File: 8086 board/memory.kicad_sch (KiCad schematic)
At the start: 49 parts, among them U10 74AC573, U11 74HC138, U12 74HC138, U13 CXK58257AM, U14 IS61C256AH, U15 IS61C256AH, U16 IS61C256AH, U17 IS61C256AH, U18 IS61C3216, U19 AM29F002, U2 74AC00, U20 AM29F002, U21 28F400B5, U3 74HC14, U8 74AC573, U9 74AC573

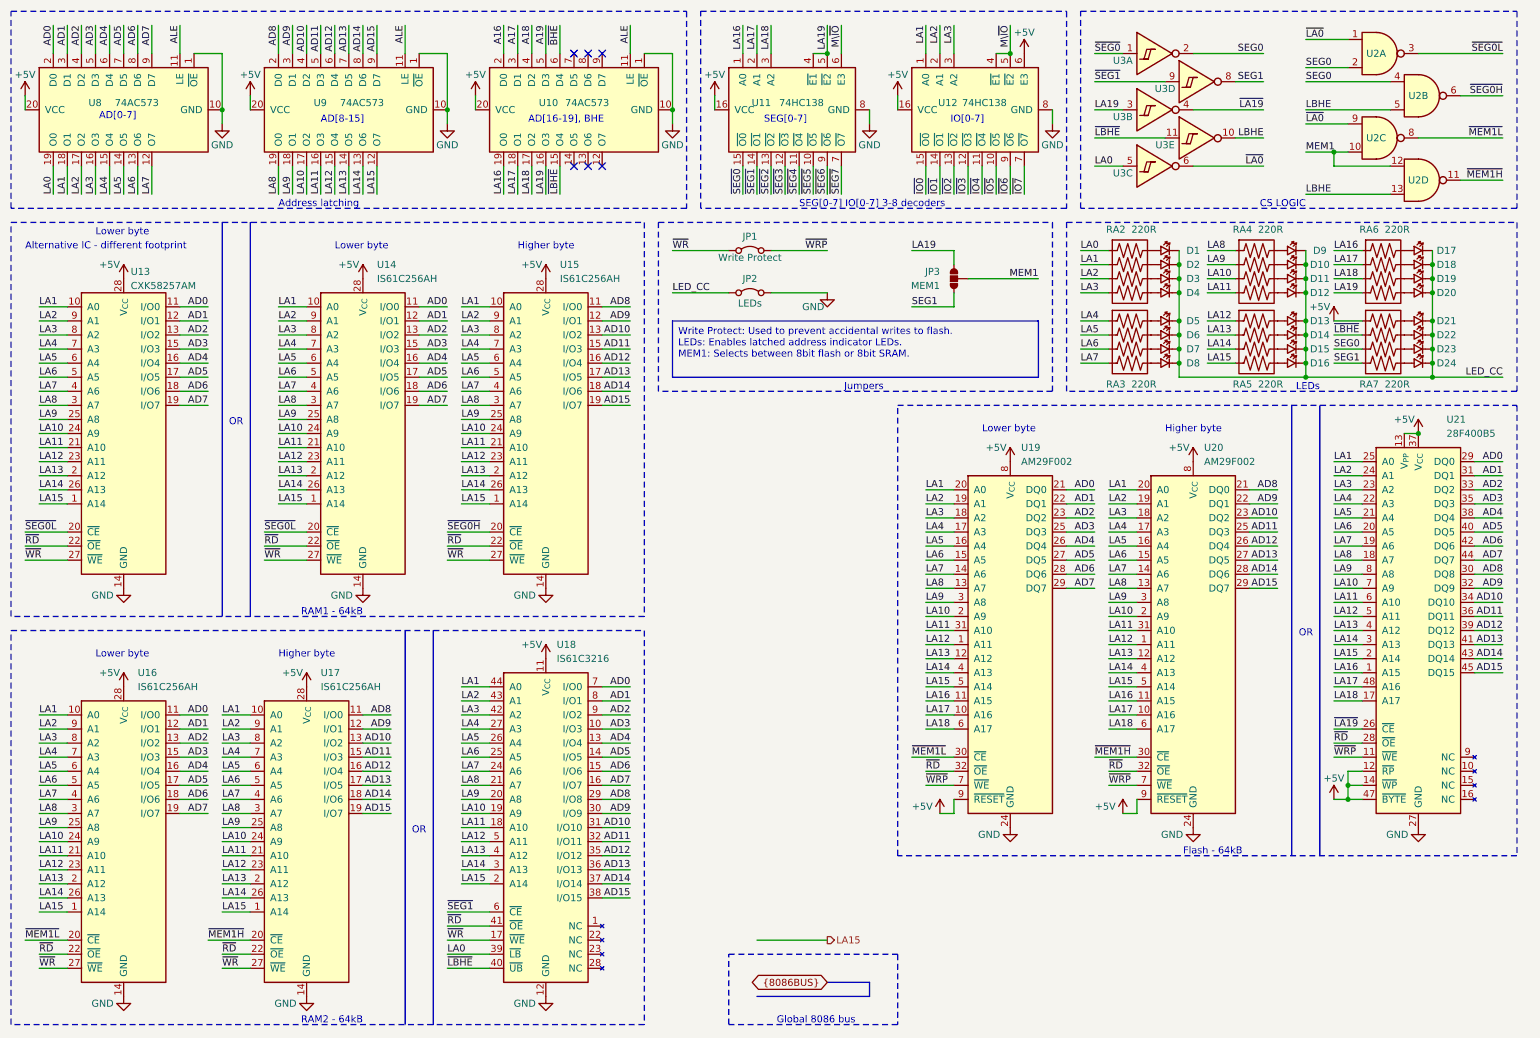
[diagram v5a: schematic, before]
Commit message: change schematic to use new components
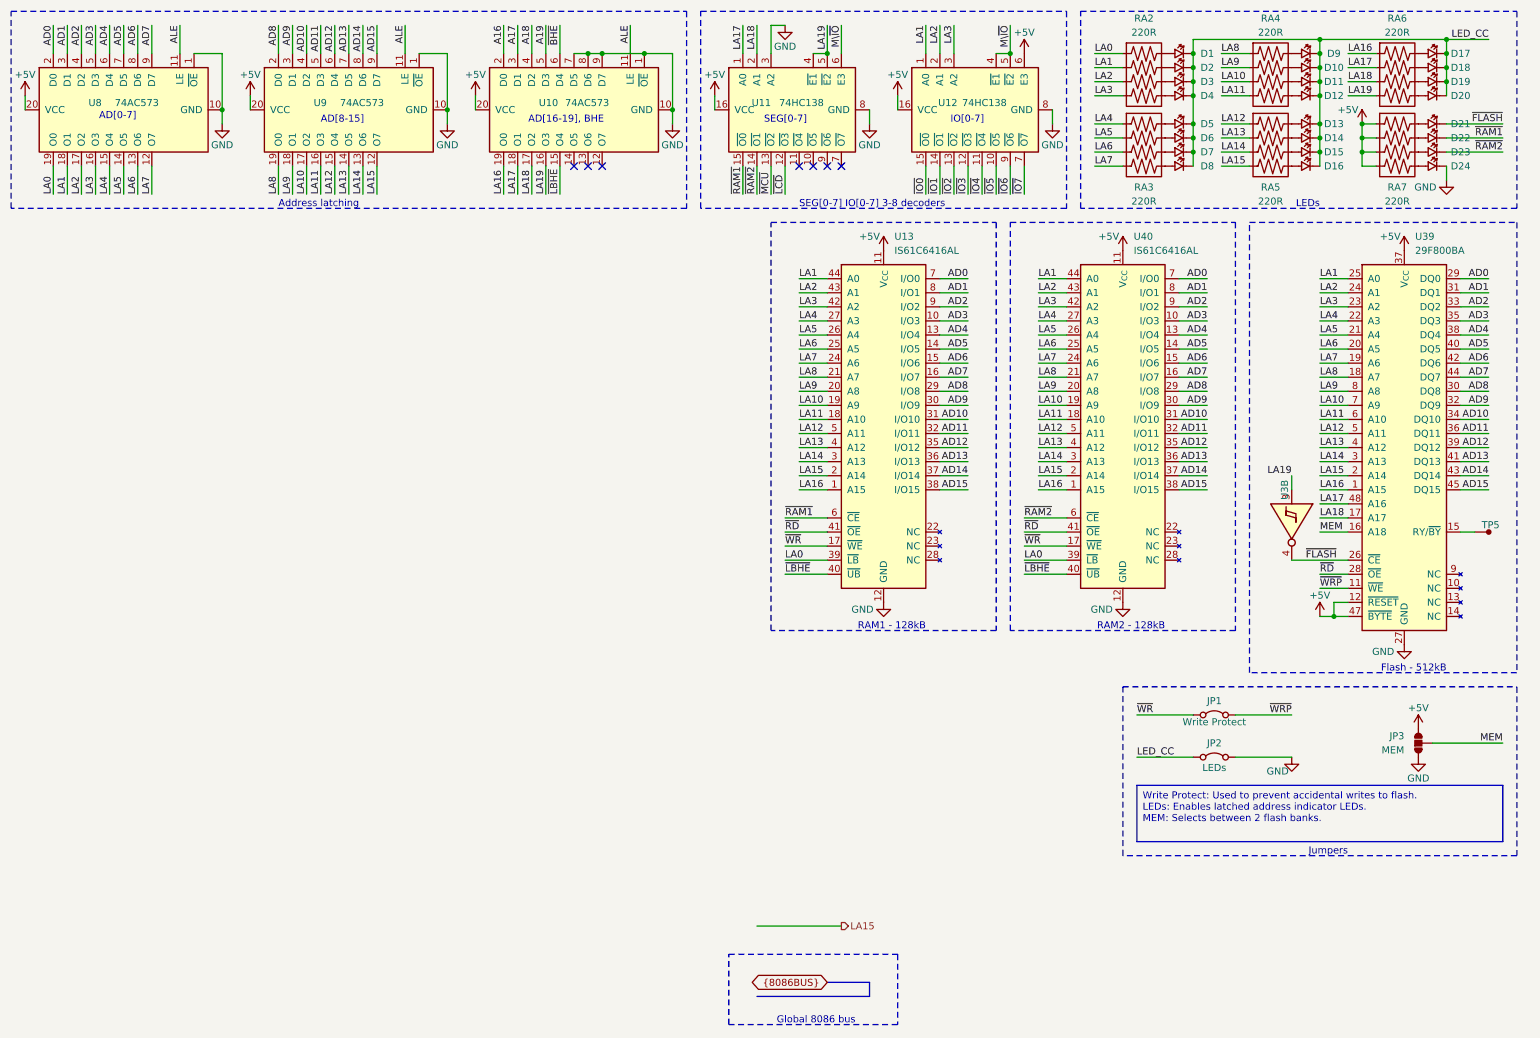
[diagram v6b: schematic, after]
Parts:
- removed U13: CXK58257AM, Package_SO:SOIC-28W_7.5x17.9mm_P1.27mm, symbol 8086PC:CXK58257AM
- removed U14, U15, U16, U17: IS61C256AH, Package_SO:TSOP-I-28_11.8x8mm_P0.55mm, symbol 8086PC:IS61C256AH
- removed U18: IS61C3216, Package_SO:TSOP-II-44_10.16x18.41mm_P0.8mm, symbol 8086PC:IS61C3216
- removed U19, U20: AM29F002, Package_SO:TSOP-I-32_18.4x8mm_P0.5mm, symbol 8086PC:AM29F002
- removed U2: 74AC00, Package_SO:SOIC-14_3.9x8.7mm_P1.27mm, symbol 8086PC:74AC00
- removed U21: 28F400B5, Package_SO:TSOP-I-48_18.4x12mm_P0.5mm, symbol 8086PC:28F400B5
- removed unit 4 of U3
- removed unit 3 of U3
- removed unit 5 of U3
- removed unit 1 of U3
- added TP5: ~, symbol 8086PC:TestPoint
- added U13, U40: IS61C6416AL, Package_SO:TSOP-II-44_10.16x18.41mm_P0.8mm, symbol 8086PC:IS61C6416
- added U39: 29F800BA, Package_SO:TSOP-I-48_18.4x12mm_P0.5mm, symbol 8086PC:29F800BA
- JP3: value MEM1 -> MEM
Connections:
- net SEG0 is gone; now on net +5V: RA7.3
- net +5V: now also JP3.2, RA7.2, RA7.4, U13.11 (V_{CC}), U13.33 (V_{CC}), U39.12 (~{RESET}), U39.37 (V_{CC}), U39.47 (~{BYTE}), U40.11 (V_{CC}), U40.33 (V_{CC})
- net AD0: now also U13.7 (I/O0), U39.29 (DQ0), U40.7 (I/O0)
- net AD1: now also U13.8 (I/O1), U39.31 (DQ1), U40.8 (I/O1)
- net AD10: now also U13.31 (I/O10), U39.34 (DQ10), U40.31 (I/O10)
- net AD11: now also U13.32 (I/O11), U39.36 (DQ11), U40.32 (I/O11)
- net AD12: now also U13.35 (I/O12), U39.39 (DQ12), U40.35 (I/O12)
- net AD13: now also U13.36 (I/O13), U39.41 (DQ13), U40.36 (I/O13)
- net AD14: now also U13.37 (I/O14), U39.43 (DQ14), U40.37 (I/O14)
- net AD15: now also U13.38 (I/O15), U39.45 (DQ15), U40.38 (I/O15)
- net AD2: now also U13.9 (I/O2), U39.33 (DQ2), U40.9 (I/O2)
- net AD3: now also U13.10 (I/O3), U39.35 (DQ3), U40.10 (I/O3)
- net AD4: now also U13.13 (I/O4), U39.38 (DQ4), U40.13 (I/O4)
- net AD5: now also U13.14 (I/O5), U39.40 (DQ5), U40.14 (I/O5)
- net AD6: now also U13.15 (I/O6), U39.42 (DQ6), U40.15 (I/O6)
- net AD7: now also U13.16 (I/O7), U39.44 (DQ7), U40.16 (I/O7)
- net AD8: now also U13.29 (I/O8), U39.30 (DQ8), U40.29 (I/O8)
- net AD9: now also U13.30 (I/O9), U39.32 (DQ9), U40.30 (I/O9)
- net GND: now also D24.2 (K), JP3.1, U10.7 (D5), U10.8 (D6), U10.9 (D7), U11.3 (A2), U13.12 (GND), U13.34 (GND), U39.27 (GND), U39.46 (GND), U40.12 (GND), U40.34 (GND)
- net LA0: now also U13.39 (~{LB}), U40.39 (~{LB})
- net LA1: now also U13.44 (A0), U39.25 (A0), U40.44 (A0)
- net LA10: now also U13.19 (A9), U39.7 (A9), U40.19 (A9)
- net LA11: now also U13.18 (A10), U39.6 (A10), U40.18 (A10)
- net LA12: now also U13.5 (A11), U39.5 (A11), U40.5 (A11)
- net LA13: now also U13.4 (A12), U39.4 (A12), U40.4 (A12)
- net LA14: now also U13.3 (A13), U39.3 (A13), U40.3 (A13)
- net LA15: now also U13.2 (A14), U39.2 (A14), U40.2 (A14)
- net LA16: now also U13.1 (A15), U39.1 (A15), U40.1 (A15); no longer U11.1 (A0)
- net LA17: now also U11.1 (A0), U39.48 (A16); no longer U11.2 (A1)
- net LA18: now also U11.2 (A1), U39.17 (A17); no longer U11.3 (A2)
- net LA19: no longer JP3.2
- net LA2: now also U13.43 (A1), U39.24 (A1), U40.43 (A1)
- net LA3: now also U13.42 (A2), U39.23 (A2), U40.42 (A2)
- net LA4: now also U13.27 (A3), U39.22 (A3), U40.27 (A3)
- net LA5: now also U13.26 (A4), U39.21 (A4), U40.26 (A4)
- net LA6: now also U13.25 (A5), U39.20 (A5), U40.25 (A5)
- net LA7: now also U13.24 (A6), U39.19 (A6), U40.24 (A6)
- net LA8: now also U13.21 (A7), U39.18 (A7), U40.21 (A7)
- net LA9: now also U13.20 (A8), U39.8 (A8), U40.20 (A8)
- net LED_CC: no longer D21.2 (K), D22.2 (K), D23.2 (K), D24.2 (K)
- net ~{LBHE}: now also U13.40 (~{UB}), U40.40 (~{UB}); no longer RA7.2
- net ~{RD}: now also U13.41 (~{OE}), U39.28 (~{OE}), U40.41 (~{OE})
- net ~{WRP}: now also U39.11 (~{WE})
- net ~{WR}: now also U13.17 (~{WE}), U40.17 (~{WE})
- net MEM1 renamed MEM
- net MEM: now also U39.16 (A18)
- removed net SEG1: JP3.1, RA7.4
- net ~{LA19} renamed ~{FLASH}
- net ~{FLASH}: now also D21.2 (K), U39.26 (~{CE})
- net ~{SEG0} renamed ~{RAM1}
- net ~{RAM1}: now also D22.2 (K), U13.6 (~{CE})
- net ~{SEG1} renamed ~{RAM2}
- net ~{RAM2}: now also D23.2 (K), U40.6 (~{CE})
- net ~{SEG2} renamed ~{MCU}
- net ~{SEG3} renamed ~{LCD}
- net ~{SEG4}: no longer names the net of U11.11 (~{O4})
- net ~{SEG5}: no longer names the net of U11.10 (~{O5})
- net ~{SEG6}: no longer names the net of U11.9 (~{O6})
- net ~{SEG7}: no longer names the net of U11.7 (~{O7})
- new net: TP5.1, U39.15 (RY/~{BY})
- no-connect marks 6 -> 7
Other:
- note added: "Flash - 512kB"
- note added: "RAM1 - 128kB"
- note added: "RAM2 - 128kB"
- note removed: "Alternative IC - different footprint"
- note removed: "CS LOGIC"
- note removed: "Flash - 64kB"
- note removed: "Higher byte"
- note removed: "Lower byte"
- note removed: "OR"
- note removed: "RAM1 - 64kB"
- note removed: "RAM2 - 64kB"
- moved on the sheet: D1, D10, D11, D12, D13, D14, D15, D16, D17, D18, D19, D2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
